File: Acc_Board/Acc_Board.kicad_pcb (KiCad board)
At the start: 2 copper layers, 152.4 x 101.6 mm, 0 parts

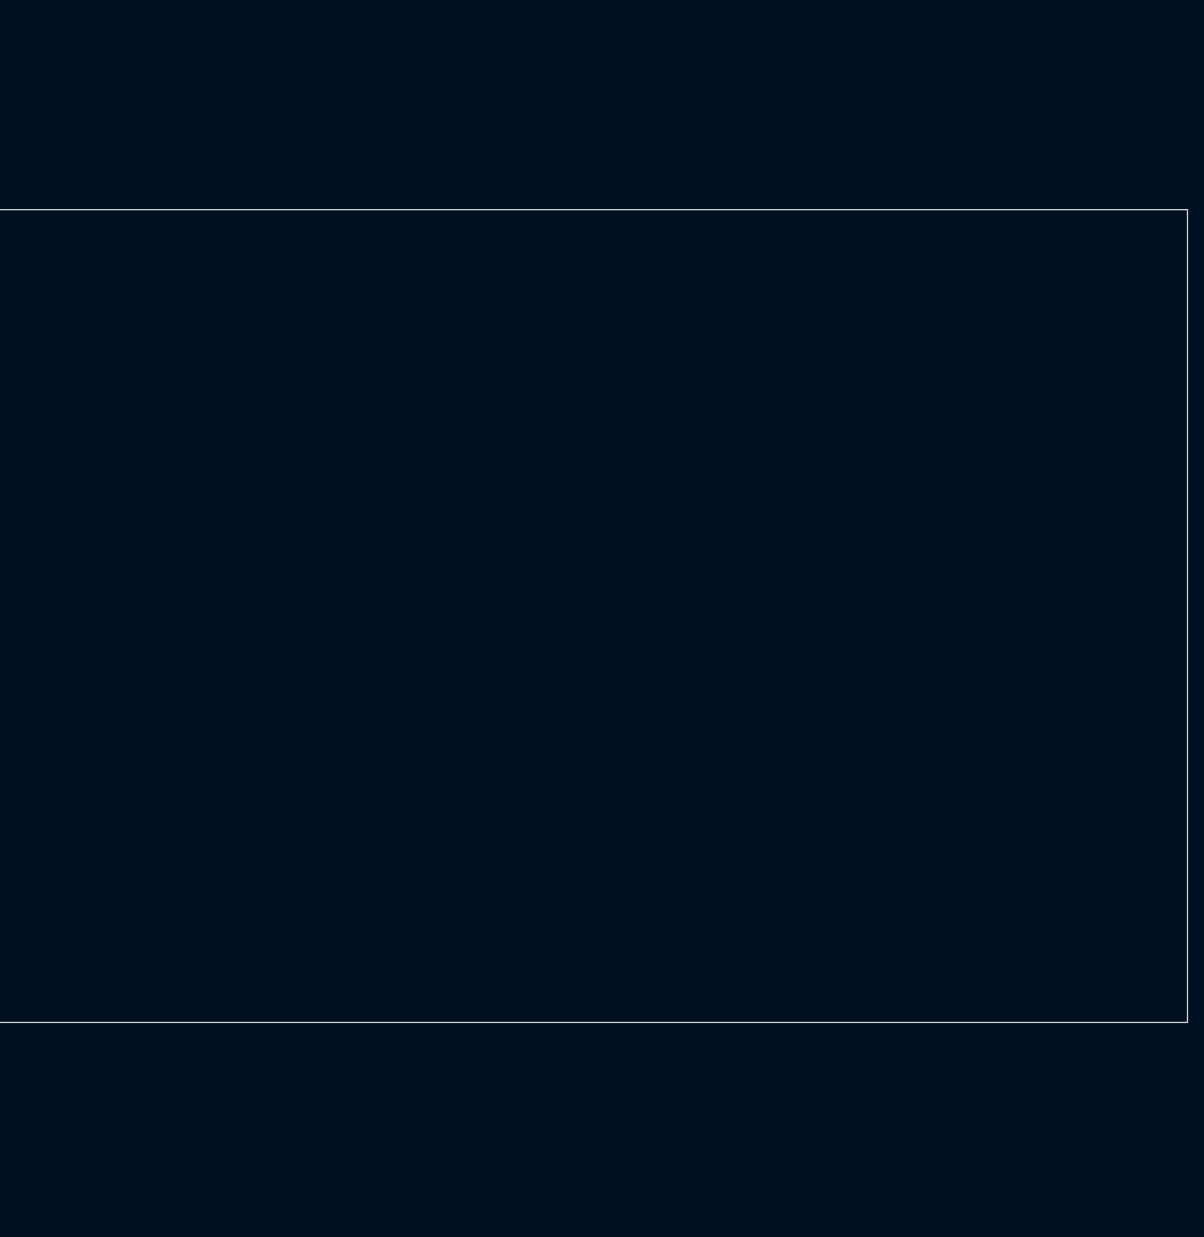
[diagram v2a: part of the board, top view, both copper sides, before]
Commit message: Changed power block and HVIL power
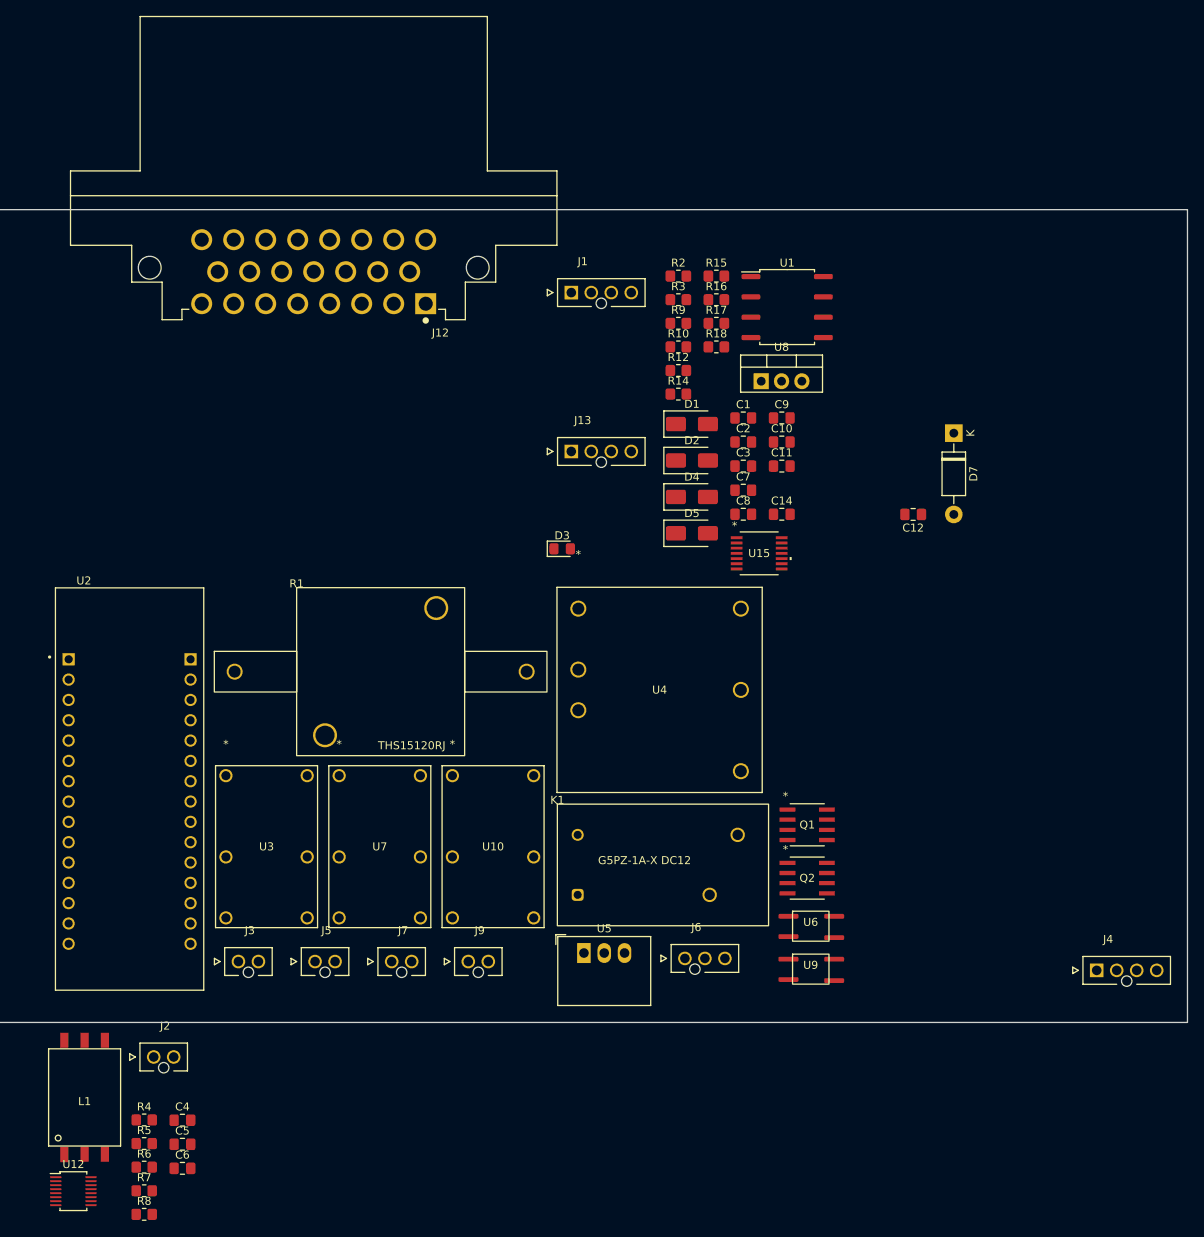
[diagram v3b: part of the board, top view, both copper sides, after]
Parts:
- added C1: 10µF, Capacitor_SMD:C_0805_2012Metric_Pad1.18x1.45mm_HandSolder, F.Cu at (109.6, 38.7)
- added C10: 100nF, Capacitor_SMD:C_0805_2012Metric_Pad1.18x1.45mm_HandSolder, F.Cu at (114.4, 41.7)
- added C11: 100nF, Capacitor_SMD:C_0805_2012Metric_Pad1.18x1.45mm_HandSolder, F.Cu at (114.4, 44.8)
- added C12: 10µF, Capacitor_SMD:C_0805_2012Metric_Pad1.18x1.45mm_HandSolder, F.Cu at (130.8, 50.8)
- added C14: 0.33µF, Capacitor_SMD:C_0805_2012Metric_Pad1.18x1.45mm_HandSolder, F.Cu at (114.4, 50.8)
- added C2: 100nF, Capacitor_SMD:C_0805_2012Metric_Pad1.18x1.45mm_HandSolder, F.Cu at (109.6, 41.7)
- added C3: 100nF, Capacitor_SMD:C_0805_2012Metric_Pad1.18x1.45mm_HandSolder, F.Cu at (109.6, 44.8)
- added C4: 10nF, Capacitor_SMD:C_0805_2012Metric_Pad1.18x1.45mm_HandSolder, F.Cu at (39.5, 126.5)
- added C5: 15pF, Capacitor_SMD:C_0805_2012Metric_Pad1.18x1.45mm_HandSolder, F.Cu at (39.5, 129.5)
- added C6: 10nF, Capacitor_SMD:C_0805_2012Metric_Pad1.18x1.45mm_HandSolder, F.Cu at (39.5, 132.5)
- added C7: 10µF, Capacitor_SMD:C_0805_2012Metric_Pad1.18x1.45mm_HandSolder, F.Cu at (109.6, 47.8)
- added C8: 0.33µF, Capacitor_SMD:C_0805_2012Metric_Pad1.18x1.45mm_HandSolder, F.Cu at (109.6, 50.8)
- added C9: 10µF, Capacitor_SMD:C_0805_2012Metric_Pad1.18x1.45mm_HandSolder, F.Cu at (114.4, 38.7)
- added D1: US1A, Diode_SMD:D_SMA, F.Cu at (103.2, 39.5)
- added D2: US1A, Diode_SMD:D_SMA, F.Cu at (103.2, 44.1)
- added D3: LED, LED_SMD:LED_0805_2012Metric_Pad1.15x1.40mm_HandSolder, F.Cu at (86.9, 55.1)
- added D4: US1A, Diode_SMD:D_SMA, F.Cu at (103.2, 48.6)
- added D5: US1A, Diode_SMD:D_SMA, F.Cu at (103.2, 53.2)
- added D7: 1N47xxA, Diode_THT:D_DO-41_SOD81_P10.16mm_Horizontal, F.Cu at (135.9, 40.6)
- added J1: AIRs Power, 1FS_2_Global_Footprint_Library:MOLEX_1053091204, F.Cu at (88.1, 23.1)
- added J12: 776087-1, 1FS_2_Global_Footprint_Library:TE_776087-1, F.Cu at (55.9, 20.5)
- added J13: Current Sensor, 1FS_2_Global_Footprint_Library:MOLEX_1053091204, F.Cu at (88.1, 42.9)
- added J2: IsoSPI, 1FS_2_Global_Footprint_Library:MOLEX_1053091202, F.Cu at (35.9, 118.6)
- added J3: IMD BAT, 1FS_2_Global_Footprint_Library:MOLEX_1053091202, F.Cu at (46.5, 106.7)
- added J4: HV Power, 1FS_2_Global_Footprint_Library:MOLEX_1053091204, F.Cu at (153.8, 107.8)
- added J5: HVIL 1, 1FS_2_Global_Footprint_Library:MOLEX_1053091202, F.Cu at (56.0, 106.7)
- added J6: IMD, 1FS_2_Global_Footprint_Library:MOLEX_1053091203, F.Cu at (102.3, 106.3)
- added J7: HVIL 2, 1FS_2_Global_Footprint_Library:MOLEX_1053091202, F.Cu at (65.6, 106.7)
- added J9: Shutdown IL, 1FS_2_Global_Footprint_Library:MOLEX_1053091202, F.Cu at (75.2, 106.7)
- added K1: Relay_SPST-NO, 1FS_2_Global_Footprint_Library:G5PZ-1A-X DC12, F.Cu at (86.3, 87.0)
- added L1: HM2113ZNL, 1FS_2_Global_Footprint_Library:HM2113ZNL, F.Cu at (27.2, 123.7)
- added Q1: STS6NF20V, 1FS_2_Global_Footprint_Library:SO-8_STM, F.Cu at (117.6, 89.6)
- added Q2: STS6NF20V, 1FS_2_Global_Footprint_Library:SO-8_STM, F.Cu at (117.6, 96.3)
- added R1: 120, 1FS_2_Global_Footprint_Library:THS15120RJ, F.Cu at (53.7, 60.0)
- added R10: 480, Resistor_SMD:R_0805_2012Metric_Pad1.20x1.40mm_HandSolder, F.Cu at (101.5, 29.9)
- added R12: 120, Resistor_SMD:R_0805_2012Metric_Pad1.20x1.40mm_HandSolder, F.Cu at (101.5, 32.8)
- added R14: 1k, Resistor_SMD:R_0805_2012Metric_Pad1.20x1.40mm_HandSolder, F.Cu at (101.5, 35.8)
- added R15: 2k, Resistor_SMD:R_0805_2012Metric_Pad1.20x1.40mm_HandSolder, F.Cu at (106.2, 21.0)
- added R16: 1k, Resistor_SMD:R_0805_2012Metric_Pad1.20x1.40mm_HandSolder, F.Cu at (106.2, 24.0)
- added R17: 2k, Resistor_SMD:R_0805_2012Metric_Pad1.20x1.40mm_HandSolder, F.Cu at (106.2, 26.9)
- added R18: 10k, Resistor_SMD:R_0805_2012Metric_Pad1.20x1.40mm_HandSolder, F.Cu at (106.2, 29.9)
- added R2: 1600, Resistor_SMD:R_0805_2012Metric_Pad1.20x1.40mm_HandSolder, F.Cu at (101.5, 21.0)
- added R3: 560, Resistor_SMD:R_0805_2012Metric_Pad1.20x1.40mm_HandSolder, F.Cu at (101.5, 24.0)
- added R4: 1.5k, Resistor_SMD:R_0805_2012Metric_Pad1.20x1.40mm_HandSolder, F.Cu at (34.7, 126.5)
- added R5: 680, Resistor_SMD:R_0805_2012Metric_Pad1.20x1.40mm_HandSolder, F.Cu at (34.7, 129.4)
- added R6: 402, Resistor_SMD:R_0805_2012Metric_Pad1.20x1.40mm_HandSolder, F.Cu at (34.7, 132.4)
- added R7: 22, Resistor_SMD:R_0805_2012Metric_Pad1.20x1.40mm_HandSolder, F.Cu at (34.7, 135.3)
- added R8: 22, Resistor_SMD:R_0805_2012Metric_Pad1.20x1.40mm_HandSolder, F.Cu at (34.7, 138.3)
- added R9: 480, Resistor_SMD:R_0805_2012Metric_Pad1.20x1.40mm_HandSolder, F.Cu at (101.5, 26.9)
- added U1: ISO1050DUB, Package_SO:SOP-8_6.62x9.15mm_P2.54mm, F.Cu at (115.1, 24.9)
- added U10: DK1A1B-12V, 1FS_2_Global_Footprint_Library:RELAY_DK2A_PAN, F.Cu at (73.2, 83.5)
- added U12: LTC6820, 1FS_2_Global_Footprint_Library:MSOP-16_[LTC6820]_10_thou_compat, F.Cu at (25.8, 135.4)
- added U15: MCP6004, 1FS_2_Global_Footprint_Library:TSSOP14_MC_MCH, F.Cu at (111.6, 55.7)
- added U2: NUCLEO-L432KC, 1FS_2_Global_Footprint_Library:MODULE_NUCLEO-L432KC, F.Cu at (32.9, 85.1)
- added U3: DK1A1B-12V, 1FS_2_Global_Footprint_Library:RELAY_DK2A_PAN, F.Cu at (44.9, 83.5)
- added U4: PQDE6W-Q110-S5-H-D, 1FS_2_Global_Footprint_Library:PQDE6W-Q110-S5-H-D_CUI, F.Cu at (89.0, 62.6)
- added U5: R-78B5.0-2.0, Converter_DCDC:Converter_DCDC_RECOM_R-78B-2.0_THT, F.Cu at (89.7, 105.6)
- added U6: NSL-32, 1FS_2_Global_Footprint_Library:OptoCoupler 6-SOP, F.Cu at (118.0, 102.3)
- added U7: DK1A1B-12V, 1FS_2_Global_Footprint_Library:RELAY_DK2A_PAN, F.Cu at (59.1, 83.5)
- added U8: LM7809_TO220, Package_TO_SOT_THT:TO-220-3_Vertical, F.Cu at (111.8, 34.1)
- added U9: NSL-32, 1FS_2_Global_Footprint_Library:OptoCoupler 6-SOP, F.Cu at (118.0, 107.6)

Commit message: Acc board changes from e meeting
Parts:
- removed J13: Current Sensor, 1FS_2_Global_Footprint_Library:MOLEX_1053091204
- J5: value HVIL 1 -> HVIL; footprint 1FS_2_Global_Footprint_Library:MOLEX_1053091202 -> 1FS_2_Global_Footprint_Library:MOLEX_1053091204
- J7: value HVIL 2 -> Current Sensor; footprint 1FS_2_Global_Footprint_Library:MOLEX_1053091202 -> 1FS_2_Global_Footprint_Library:MOLEX_1053091204
- moved U15 162.4 mm to (270.9, 24.6)
- moved C1 155.9 mm to (265.5, 41.5)
- moved C10 155.9 mm to (270.3, 44.5)
- moved C11 155.9 mm to (270.3, 47.5)
- moved C14 155.9 mm to (270.3, 53.6)
- moved C2 155.9 mm to (265.5, 44.5)
- moved C3 155.9 mm to (265.5, 47.5)
- moved C7 155.9 mm to (265.5, 50.6)
- moved C8 155.9 mm to (265.5, 53.6)
- moved C9 155.9 mm to (270.3, 41.5)
- moved J6 155.9 mm to (258.2, 109.1)
- moved Q1 155.9 mm to (273.5, 92.4)
- moved Q2 155.9 mm to (273.5, 99.1)
- moved R10 155.9 mm to (257.3, 32.6)
- moved R14 155.9 mm to (257.3, 38.5)
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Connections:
- J7 pad 2: /HVIL+ -> +5V
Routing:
- net /CAN_L: track 0.00 -> 10.8 mm
- net /CAN_H: track 0.00 -> 10.2 mm
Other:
- board size 152.4 x 101.6 mm -> 127 x 101.6 mm

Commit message: traces for acc board, WIP
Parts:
- added J8: Fans, 1FS_2_Global_Footprint_Library:MOLEX_1053091206, F.Cu at (139.6, 19.2)
- added Q3: STS6NF20V, 1FS_2_Global_Footprint_Library:SO-8_STM, F.Cu at (120.7, 25.4)
- added R11: 120, Resistor_SMD:R_0805_2012Metric_Pad1.20x1.40mm_HandSolder, F.Cu at (59.7, 49.5)
- added REF**: MountingHole_2.2mm_M2, MountingHole:MountingHole_2.2mm_M2, F.Cu at (147.3, 17.8)
- added REF**: MountingHole_2.2mm_M2, MountingHole:MountingHole_2.2mm_M2, F.Cu at (17.8, 83.8)
- added REF**: MountingHole_2.2mm_M2, MountingHole:MountingHole_2.2mm_M2, F.Cu at (17.8, 17.8)
- R10, R9: value 480 -> 370
- moved U9 255.8 mm to (25.4, 49.5)
- moved C14 244.0 mm to (27.9, 25.4)
- moved R9 239.2 mm to (19.1, 50.8)
- moved C8 237.9 mm to (30.5, 16.5), turned to 180 degrees
- moved D5 233.6 mm to (25.4, 54.6), turned to 180 degrees
- moved U6 227.4 mm to (53.3, 49.5)
- moved Q2 224.4 mm to (49.5, 85.1)
- moved D4 220.9 mm to (39.4, 74.9), turned to 180 degrees
- moved R10 211.1 mm to (47.0, 50.8), turned to 180 degrees
- moved R2 211.0 mm to (55.9, 86.4), turned to -90 degrees
- moved Q1 209.3 mm to (64.8, 76.2)
- moved R3 209.0 mm to (55.9, 82.5), turned to -90 degrees
- moved D2 205.8 mm to (53.3, 54.6), turned to 180 degrees
- moved C10 199.5 mm to (71.4, 29.2), turned to 180 degrees
- moved C11 199.2 mm to (71.1, 44.5), turned to 180 degrees
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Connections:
- net Net-(U1-RXD) renamed /CAN1_RD
- net Net-(U1-TXD) renamed /CAN1_TD
- U2 pad CN3_12: unconnected-(U2A-PA8-PadCN3_12) -> Net-(U2A-PA8)
- U2 pad CN3_3: Net-(D3-A) -> unconnected-(U2A-NRST-PadCN3_3)
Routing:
- net GND: track 0.00 -> 426.6 mm, vias 0 -> 9
- net +12V: track 0.00 -> 250.4 mm, vias 0 -> 3
- net /Shutdown_ACC_OUT: track 0.00 -> 114.8 mm, vias 0 -> 2
- net +5V: track 0.00 -> 93.2 mm, vias 0 -> 2
- net /Shutdown_ACC_IN: track 0.00 -> 92.1 mm, vias 0 -> 4
- net /Current_Vref: track 0.00 -> 81.5 mm, vias 0 -> 5
- net /Current_Output: track 0.00 -> 75.5 mm
- net +3.3V: track 0.00 -> 69.2 mm, vias 0 -> 4
- net /Iso SPI/STM_NSS: track 0.00 -> 63.2 mm
- net Net-(U2A-PA3): track 0.00 -> 50.1 mm, vias 0 -> 2
- net /HVIL+: track 0.00 -> 49.3 mm
- net /Iso SPI/STM_SCK: track 0.00 -> 49.2 mm, vias 0 -> 1
- net /BAT+: track 0.00 -> 44.7 mm
- net /CAN1_TD: track 0.00 -> 41.7 mm, vias 0 -> 1
- net Net-(U2A-PA1): track 0.00 -> 41.3 mm, vias 0 -> 2
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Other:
- board size 127 x 101.6 mm -> 139.7 x 76.2 mm
- board text added: "GLV"
- board text added: "TS"

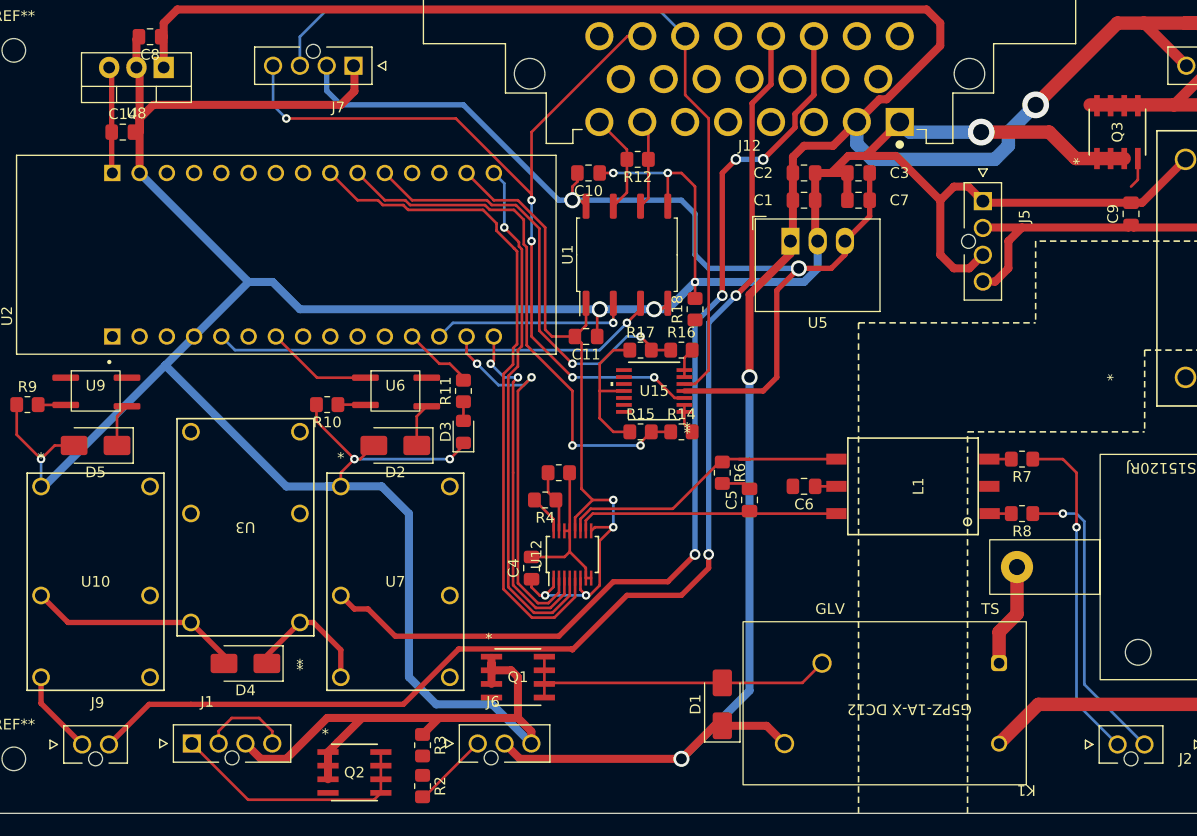
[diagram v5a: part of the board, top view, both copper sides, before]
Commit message: more traces and fan control for acc board
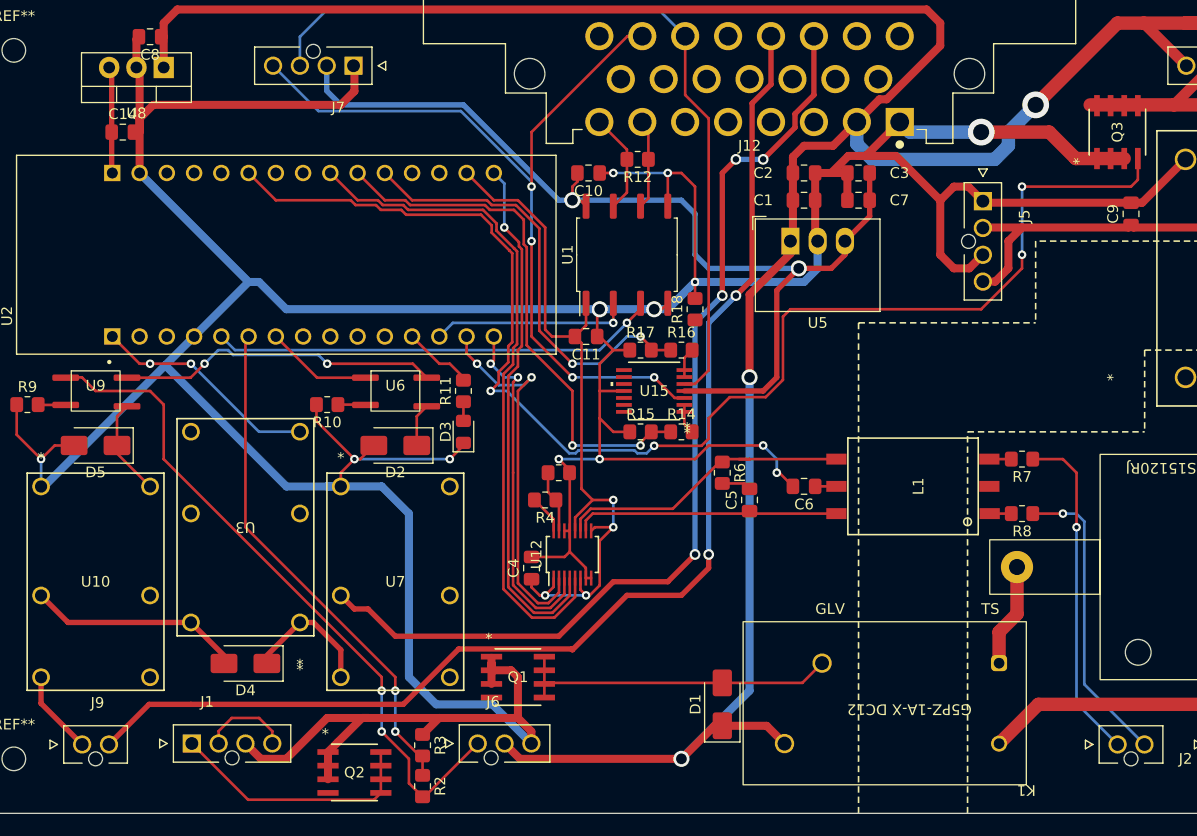
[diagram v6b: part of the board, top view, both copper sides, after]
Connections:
- U2 pad CN4_6: unconnected-(U2A-PA7-PadCN4_6) -> /Fan_Control
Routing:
- net /Fan_Control: track 2.88 -> 126.3 mm, vias 0 -> 4
- net /IMD_FAULT: track 7.20 -> 64.0 mm, vias 0 -> 2
- net /IMD_Status: track 0.00 -> 48.0 mm, vias 0 -> 2
- net GND: track 426.6 -> 458.8 mm, vias 9 -> 13
- net +12V: track 250.4 -> 280.4 mm, vias 3 -> 5
- net /Charge_Enable: track 0.00 -> 21.2 mm, vias 0 -> 2
- net Net-(D5-K): track 4.04 -> 9.14 mm
- net /Current_Vref: track 81.5 -> 78.7 mm, vias 5 -> 4

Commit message: Acc board traces done (for now)
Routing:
- net /IMD_FAULT: track 64.0 -> 170.7 mm, vias 2 -> 3
- net /AIRS+_12V: track 8.32 -> 113.8 mm, vias 0 -> 4
- net /BMS_FAULT: track 9.94 -> 108.6 mm, vias 0 -> 1
- net /Charge_Exit: track 0.00 -> 88.6 mm, vias 0 -> 4
- net /Charge_State: track 0.00 -> 86.1 mm, vias 0 -> 2
- net /Precharge_Control: track 0.00 -> 60.9 mm, vias 0 -> 3
- net +12V: track 280.4 -> 330.7 mm, vias 5 -> 6
- net /Precharge_Relay: track 0.00 -> 45.1 mm, vias 0 -> 2
- net GND: track 458.8 -> 465.7 mm, vias 13 -> 11
- net Net-(J8-Pad1): track 33.3 -> 39.7 mm
- net Net-(D2-K): track 4.04 -> 9.14 mm
- net /Current_Output: track 75.5 -> 77.8 mm
- net /Charge_Enable: vias 2 -> 1
